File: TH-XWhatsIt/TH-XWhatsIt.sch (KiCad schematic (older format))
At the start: 28 parts, among them J1 MODEL F, J2 EXPANSION, J3 EXPANSION HEADER, SW1 SW_Push, SW2 SW_Push, U1 MCP4921-EP, U2 LM339, U3 74HCT595, U4 74HCT595, U5 ProMicro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

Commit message: Added compact beamspring-only version
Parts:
- removed C7: 0U1, Capacitor_SMD:C_0402_1005Metric, symbol Device:C_Small
- removed H1, H2: GROUND STRAP, MountingHole:MountingHole_4.5mm_Pad_Via, symbol Mechanical:MountingHole_Pad
- removed J2: EXPANSION, TH-XWhatsIt:12-pin-castelated-connector, symbol Connector_Generic:Conn_01x12
- removed RN3: 100K, Resistor_SMD:R_Array_Convex_4x0603, symbol Device:R_Pack04
- removed SW1, SW2: SW_Push, TH-XWhatsIt:PadsToShort, symbol Switch:SW_Push
- removed U6: LM339, Package_SO:SOIC-14_3.9x8.7mm_P1.27mm, symbol Comparator:LM339
- added NT1, NT2: Net-Tie_3, NetTie:NetTie-3_THT_Pad0.3mm, symbol Device:Net-Tie_3
- C1, C2, C3, C4, C5, C6: footprint Capacitor_SMD:C_0402_1005Metric -> Capacitor_SMD:C_0805_2012Metric_Pad1.15x1.40mm_HandSolder
- J1: value MODEL F -> BEAMSPRING CONNECTOR; footprint TH-XWhatsIt:30-pin-castelated-connector -> TH-XWhatsIt:30-pin-universal-beamspring-connector_v2
- R1, R2, R3, R4, R5: footprint Resistor_SMD:R_0402_1005Metric -> Resistor_SMD:R_0805_2012Metric_Pad1.15x1.40mm_HandSolder
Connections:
- net labels removed: COL24, SENSE5, SENSE6, SENSE7, SENSE8
- wire segments 111 -> 78
- no-connect marks 2 -> 4
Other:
- moved on the sheet: J3

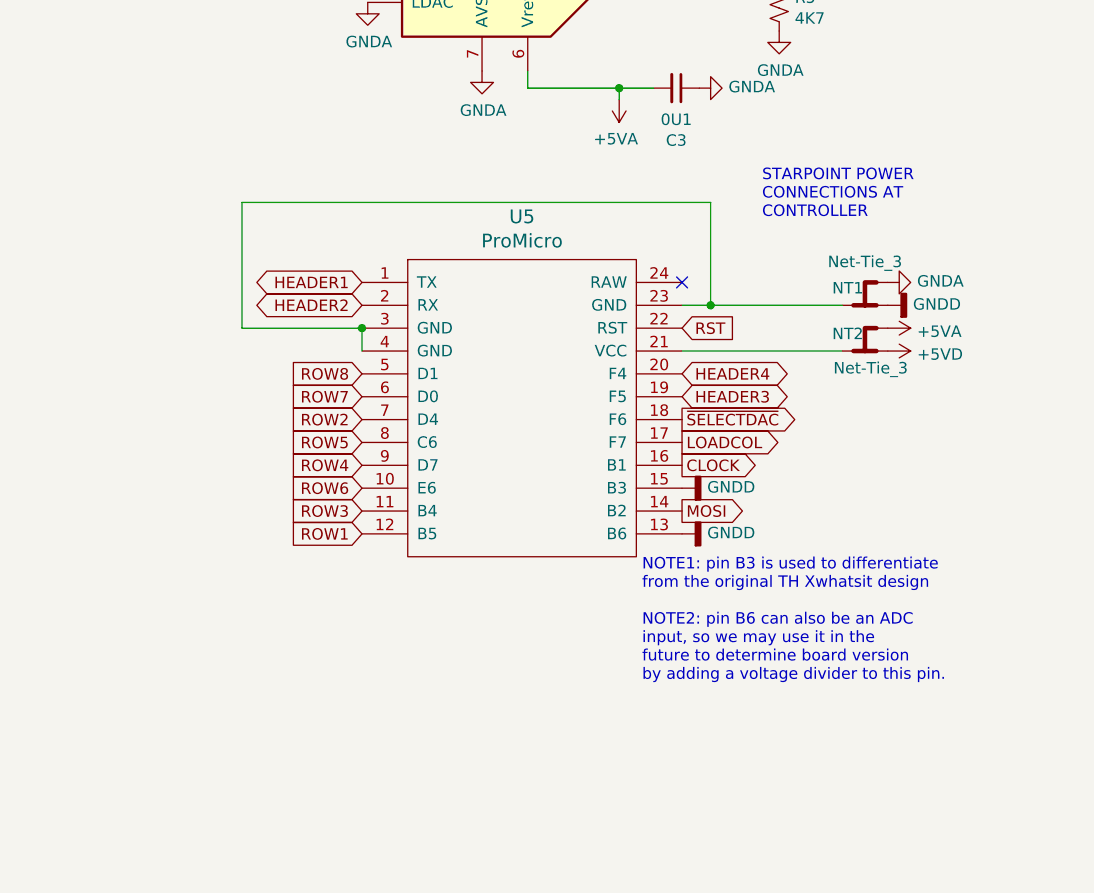
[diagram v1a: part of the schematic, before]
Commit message: added version selection resistor divider pads
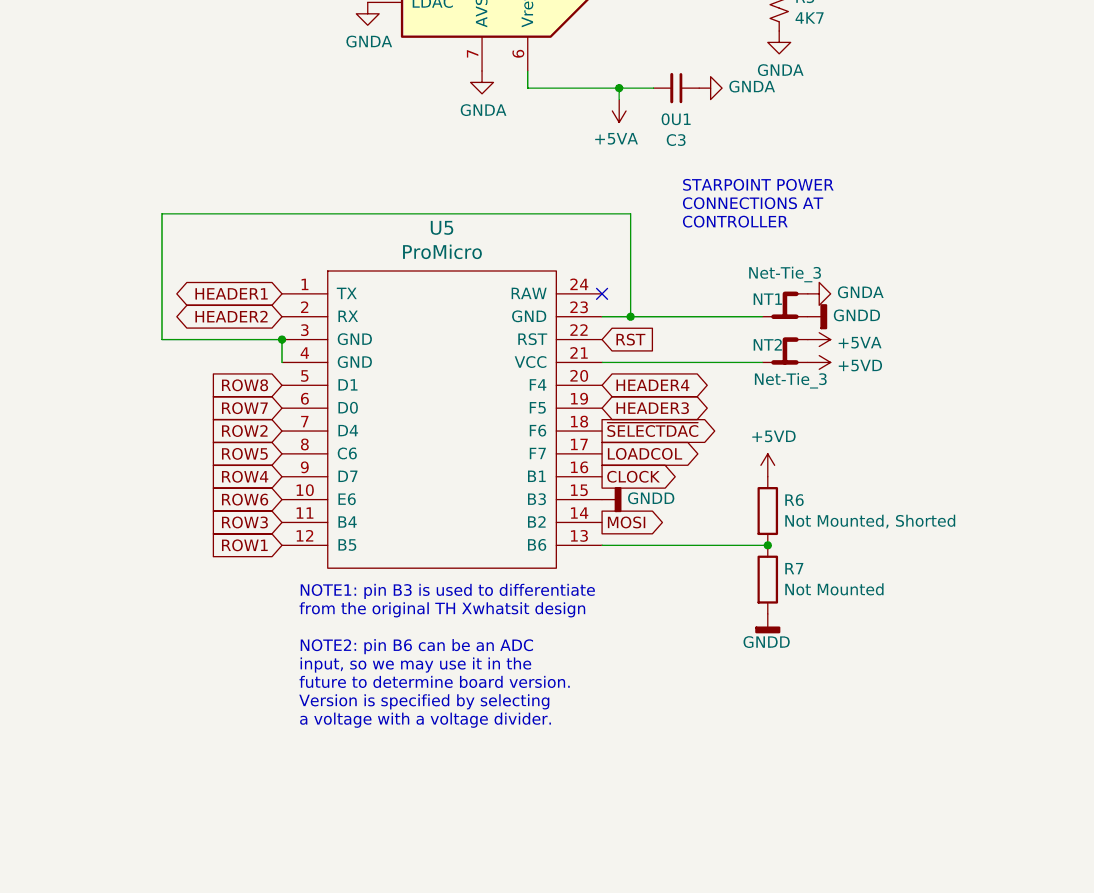
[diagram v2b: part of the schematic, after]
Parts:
- added R6: Not Mounted, Shorted, TH-XWhatsIt:SHORTEDR_0805_2012Metric_Pad1.15x1.40mm_HandSolder, symbol Device:R
- added R7: Not Mounted, Resistor_SMD:R_0805_2012Metric_Pad1.15x1.40mm_HandSolder, symbol Device:R
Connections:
- net +5VD: now also R6.1
- net GNDD: now also R7.2; no longer U5.13 (B6)
- new net: R6.2, R7.1, U5.13 (B6)
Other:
- note added: "NOTE1: pin B3 is used to differentiate\nfrom the original TH Xwhatsit design\n\nNOTE2: pin B6 can be an ADC\ninput, so we may use it in the\nfuture to determine board version.\nVersion is specified by selecting\na voltage with a voltage divider."
- note removed: "NOTE1: pin B3 is used to differentiate\nfrom the original TH Xwhatsit design\n\nNOTE2: pin B6 can also be an ADC\ninput, so we may use it in the\nfuture to determine board version\nby adding a voltage divider to this pin."
- moved on the sheet: NT1, NT2, U5
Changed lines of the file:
@@
 Wire Wire Line
 	10275 1400 10275 1425
-Text GLabel 9850 3525 2    50   Output ~ 0
+Text GLabel 9500 3575 2    50   Output ~ 0
 CLOCK
-NoConn ~ 9850 2725
-Text GLabel 8450 3825 0    50   Input ~ 0
+NoConn ~ 9500 2775
+Text GLabel 8100 3875 0    50   Input ~ 0
 ROW1
-Text GLabel 8450 3325 0    50   Input ~ 0
+Text GLabel 8100 3375 0    50   Input ~ 0
 ROW2
-Text GLabel 8450 3725 0    50   Input ~ 0
+Text GLabel 8100 3775 0    50   Input ~ 0
 ROW3
-Text GLabel 8450 3525 0    50   Input ~ 0
+Text GLabel 8100 3575 0    50   Input ~ 0
 ROW4
-Text GLabel 8450 3425 0    50   Input ~ 0
+Text GLabel 8100 3475 0    50   Input ~ 0
 ROW5
-Text GLabel 8450 3625 0    50   Input ~ 0
+Text GLabel 8100 3675 0    50   Input ~ 0
 ROW6
-Text GLabel 8450 3225 0    50   Input ~ 0
+Text GLabel 8100 3275 0    50   Input ~ 0
 ROW7
-Text GLabel 8450 3125 0    50   Input ~ 0
+Text GLabel 8100 3175 0    50   Input ~ 0
 ROW8
 $Comp
@@
 Text GLabel 3500 2775 2    50   Output ~ 0
 ROW4
-Text GLabel 9850 3425 2    50   Output ~ 0
+Text GLabel 9500 3475 2    50   Output ~ 0
 LOADCOL
 Text GLabel 2675 5875 0    50   Input ~ 0
@@
 Text GLabel 2675 5375 0    50   Input ~ 0
 COL14
-Text GLabel 9850 3725 2    50   Output ~ 0
+Text GLabel 9500 3775 2    50   Output ~ 0
 MOSI
 Text GLabel 8475 1200 0    50   Input ~ 0
@@
 	1    0    0    -1
 $EndComp
-Text GLabel 9850 3325 2    50   Output ~ 0
+Text GLabel 9500 3375 2    50   Output ~ 0
 ~SELECTDAC
 Text GLabel 8475 1400 0    50   Input ~ 0
@@
 L power:+5VD #PWR027
 U 1 1 5E81915B
-P 10750 3025
-F 0 "#PWR027" H 10750 2875 50  0001 C CNN
-F 1 "+5VD" V 10765 3153 50  0000 L CNN
-F 2 "" H 10750 3025 50  0001 C CNN
-F 3 "" H 10750 3025 50  0001 C CNN
-	1    10750 3025
+P 10400 3075
+F 0 "#PWR027" H 10400 2925 50  0001 C CNN
+F 1 "+5VD" V 10415 3203 50  0000 L CNN
+F 2 "" H 10400 3075 50  0001 C CNN
+F 3 "" H 10400 3075 50  0001 C CNN
+	1    10400 3075
 	0    1    1    0
 $EndComp
@@
 L power:GNDD #PWR023
 U 1 1 5E823659
-P 10750 2825
-F 0 "#PWR023" H 10750 2575 50  0001 C CNN
-F 1 "GNDD" V 10754 2715 50  0000 R CNN
-F 2 "" H 10750 2825 50  0001 C CNN
-F 3 "" H 10750 2825 50  0001 C CNN
-	1    10750 2825
+P 10400 2875
+F 0 "#PWR023" H 10400 2625 50  0001 C CNN
+F 1 "GNDD" V 10404 2765 50  0000 R CNN
+F 2 "" H 10400 2875 50  0001 C CNN
+F 3 "" H 10400 2875 50  0001 C CNN
+	1    10400 2875
 	0    -1   -1   0
 $EndComp
@@
 L power:+5VA #PWR025
 U 1 1 5E8BFA71
-P 10750 2925
-F 0 "#PWR025" H 10750 2775 50  0001 C CNN
-F 1 "+5VA" V 10765 3053 50  0000 L CNN
-F 2 "" H 10750 2925 50  0001 C CNN
-F 3 "" H 10750 2925 50  0001 C CNN
-	1    10750 2925
+P 10400 2975
+F 0 "#PWR025" H 10400 2825 50  0001 C CNN
+F 1 "+5VA" V 10415 3103 50  0000 L CNN
+F 2 "" H 10400 2975 50  0001 C CNN
+F 3 "" H 10400 2975 50  0001 C CNN
+	1    10400 2975
 	0    1    1    0
 $EndComp
@@
 L power:GNDA #PWR021
 U 1 1 5E8BFD09
-P 10750 2725
-F 0 "#PWR021" H 10750 2475 50  0001 C CNN
-F 1 "GNDA" V 10755 2597 50  0000 R CNN
-F 2 "" H 10750 2725 50  0001 C CNN
-F 3 "" H 10750 2725 50  0001 C CNN
-	1    10750 2725
-	0    -1   -1   0
-$EndComp
-Wire Wire Line
-	9850 3025 10550 3025
-Wire Wire Line
-	10550 2825 9975 2825
-Text Notes 10200 2450 0    50   ~ 0
+P 10400 2775
+F 0 "#PWR021" H 10400 2525 50  0001 C CNN
+F 1 "GNDA" V 10405 2647 50  0000 R CNN
+F 2 "" H 10400 2775 50  0001 C CNN
+F 3 "" H 10400 2775 50  0001 C CNN
+	1    10400 2775
+	0    -1   -1   0
+$EndComp
+Wire Wire Line
+	9500 3075 10200 3075
+Wire Wire Line
+	10200 2875 9625 2875
+Text Notes 9850 2500 0    50   ~ 0
 STARPOINT POWER\nCONNECTIONS AT\nCONTROLLER
 Text GLabel 2675 3875 0    50   Output ~ 0
@@
 Text GLabel 7125 6100 2    50   BiDi ~ 0
 HEADER4
-Text GLabel 8450 2725 0    50   BiDi ~ 0
+Text GLabel 8100 2775 0    50   BiDi ~ 0
 HEADER1
-Text GLabel 8450 2825 0    50   BiDi ~ 0
+Text GLabel 8100 2875 0    50   BiDi ~ 0
 HEADER2
-Text GLabel 9850 3225 2    50   BiDi ~ 0
+Text GLabel 9500 3275 2    50   BiDi ~ 0
 HEADER3
-Text GLabel 9850 3125 2    50   BiDi ~ 0
+Text GLabel 9500 3175 2    50   BiDi ~ 0
 HEADER4
 Text GLabel 6625 6200 0    50   BiDi ~ 0
@@
 L power:GNDD #PWR0103
 U 1 1 5F4E8027
-P 9850 3625
-F 0 "#PWR0103" H 9850 3375 50  0001 C CNN
-F 1 "GNDD" V 9854 3515 50  0000 R CNN
-F 2 "" H 9850 3625 50  0001 C CNN
-F 3 "" H 9850 3625 50  0001 C CNN
-	1    9850 3625
+P 9500 3675
+F 0 "#PWR0103" H 9500 3425 50  0001 C CNN
+F 1 "GNDD" V 9504 3565 50  0000 R CNN
+F 2 "" H 9500 3675 50  0001 C CNN
+F 3 "" H 9500 3675 50  0001 C CNN
+	1    9500 3675
 	0    -1   -1   0
 $EndComp
@@
 L promicro:ProMicro U5
 U 1 1 5E3248FF
-P 9150 3475
-F 0 "U5" H 9150 4512 60  0000 C CNN
-F 1 "ProMicro" H 9150 4406 60  0000 C CNN
-F 2 "promicro:ProMicro" H 9250 2425 60  0001 C CNN
-F 3 "" H 9250 2425 60  0000 C CNN
-	1    9150 3475
+P 8800 3525
+F 0 "U5" H 8800 4562 60  0000 C CNN
+F 1 "ProMicro" H 8800 4456 60  0000 C CNN
+F 2 "promicro:ProMicro" H 8900 2475 60  0001 C CNN
+F 3 "" H 8900 2475 60  0000 C CNN
+	1    8800 3525
 	1    0    0    -1
 $EndComp
@@
 L power:GNDD #PWR0107
 U 1 1 5F3A2D72
-P 9850 3825
-F 0 "#PWR0107" H 9850 3575 50  0001 C CNN
-F 1 "GNDD" V 9854 3715 50  0000 R CNN
-F 2 "" H 9850 3825 50  0001 C CNN
-F 3 "" H 9850 3825 50  0001 C CNN
-	1    9850 3825
-	0    -1   -1   0
-$EndComp
-Text Notes 9675 4475 0    50   ~ 0
-NOTE1: pin B3 is used to differentiate\nfrom the original TH Xwhatsit design\n\nNOTE2: pin B6 can also be an ADC\ninput, so we may use it in the\nfuture to determine board version\nby adding a voltage divider to this pin.
-Text GLabel 9850 2925 2    50   Input ~ 0
+P 10225 4175
+F 0 "#PWR0107" H 10225 3925 50  0001 C CNN
+F 1 "GNDD" H 10325 4050 50  0000 R CNN
+F 2 "" H 10225 4175 50  0001 C CNN
+F 3 "" H 10225 4175 50  0001 C CNN
+	1    10225 4175
+	1    0    0    -1
+$EndComp
+Text Notes 8175 4675 0    50   ~ 0
+NOTE1: pin B3 is used to differentiate\nfrom the original TH Xwhatsit design\n\nNOTE2: pin B6 can be an ADC\ninput, so we may use it in the\nfuture to determine board version.\nVersion is specified by selecting\na voltage with a voltage divider.
+Text GLabel 9500 2975 2    50   Input ~ 0
 RST
 $Comp
@@
 L Device:Net-Tie_3 NT1
 U 1 1 5F6D07D8
-P 10650 2825
-F 0 "NT1" H 10725 2750 50  0000 C CNN
-F 1 "Net-Tie_3" H 10650 2635 50  0000 C CNN
-F 2 "NetTie:NetTie-3_THT_Pad0.3mm" H 10650 2825 50  0001 C CNN
-F 3 "~" H 10650 2825 50  0001 C CNN
-	1    10650 2825
+P 10300 2875
+F 0 "NT1" H 10375 2800 50  0000 C CNN
+F 1 "Net-Tie_3" H 10300 2685 50  0000 C CNN
+F 2 "NetTie:NetTie-3_THT_Pad0.3mm" H 10300 2875 50  0001 C CNN
+F 3 "~" H 10300 2875 50  0001 C CNN
+	1    10300 2875
 	-1   0    0    1
 $EndComp
@@
 L Device:Net-Tie_3 NT2
 U 1 1 5F6D1B28
-P 10650 3025
-F 0 "NT2" H 10725 2950 50  0000 C CNN
-F 1 "Net-Tie_3" H 10625 3100 50  0000 C CNN
-F 2 "NetTie:NetTie-3_THT_Pad0.3mm" H 10650 3025 50  0001 C CNN
-F 3 "~" H 10650 3025 50  0001 C CNN
-	1    10650 3025
+P 10300 3075
+F 0 "NT2" H 10375 3000 50  0000 C CNN
+F 1 "Net-Tie_3" H 10275 3150 50  0000 C CNN
+F 2 "NetTie:NetTie-3_THT_Pad0.3mm" H 10300 3075 50  0001 C CNN
+F 3 "~" H 10300 3075 50  0001 C CNN
+	1    10300 3075
 	-1   0    0    1
 $EndComp
 Wire Wire Line
-	8450 3025 8450 2925
-Wire Wire Line
-	8450 2925 7925 2925
-Wire Wire Line
-	7925 2925 7925 2375
-Wire Wire Line
-	7925 2375 9975 2375
-Wire Wire Line
-	9975 2375 9975 2825
-Connection ~ 8450 2925
-Connection ~ 9975 2825
-Wire Wire Line
-	9975 2825 9850 2825
+	8100 3075 8100 2975
+Wire Wire Line
+	8100 2975 7575 2975
+Wire Wire Line
+	7575 2975 7575 2425
+Wire Wire Line
+	7575 2425 9625 2425
+Wire Wire Line
+	9625 2425 9625 2875
+Connection ~ 8100 2975
+Connection ~ 9625 2875
+Wire Wire Line
+	9625 2875 9500 2875
+$Comp
+L Device:R R6
+U 1 1 5F3A43C9
+P 10225 3725
+F 0 "R6" H 10295 3771 50  0000 L CNN
+F 1 "Not Mounted, Shorted" H 10295 3680 50  0000 L CNN
+F 2 "TH-XWhatsIt:SHORTEDR_0805_2012Metric_Pad1.15x1.40mm_HandSolder" V 10155 3725 50  0001 C CNN
+F 3 "~" H 10225 3725 50  0001 C CNN
+	1    10225 3725
+	1    0    0    -1
+$EndComp
+$Comp
+L Device:R R7
+U 1 1 5F3A4C74
+P 10225 4025
+F 0 "R7" H 10295 4071 50  0000 L CNN
+F 1 "Not Mounted" H 10295 3980 50  0000 L CNN
+F 2 "Resistor_SMD:R_0805_2012Metric_Pad1.15x1.40mm_HandSolder" V 10155 4025 50  0001 C CNN
+F 3 "~" H 10225 4025 50  0001 C CNN
+	1    10225 4025
+	1    0    0    -1
+$EndComp
+Wire Wire Line
+	10225 3875 9500 3875
+Connection ~ 10225 3875
+$Comp
+L power:+5VD #PWR04
+U 1 1 5F3A9745
+P 10225 3575
+F 0 "#PWR04" H 10225 3425 50  0001 C CNN
+F 1 "+5VD" H 10150 3750 50  0000 L CNN
+F 2 "" H 10225 3575 50  0001 C CNN
+F 3 "" H 10225 3575 50  0001 C CNN
+	1    10225 3575
+	1    0    0    -1
+$EndComp
 $EndSCHEMATC

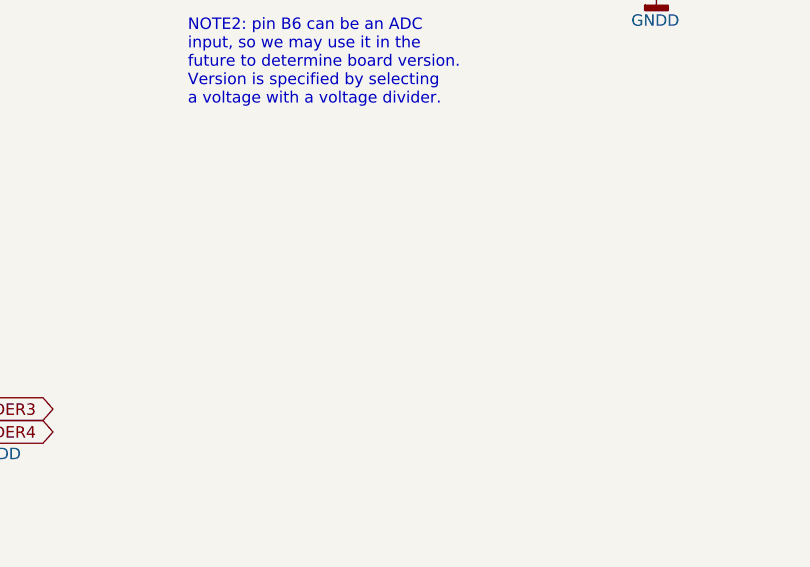
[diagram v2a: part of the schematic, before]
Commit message: Added chassis ground, and added some silkscreen
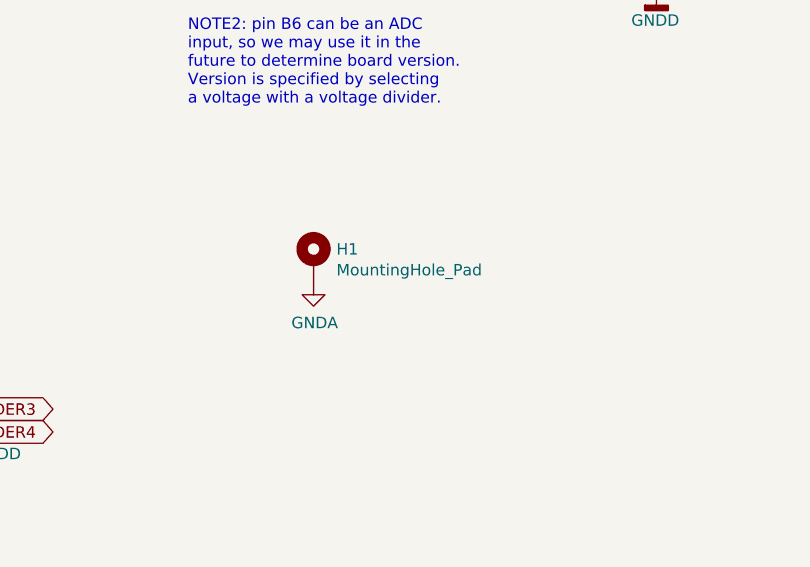
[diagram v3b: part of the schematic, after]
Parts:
- added H1: MountingHole_Pad, TH-XWhatsIt:ChassisGnd, symbol Mechanical:MountingHole_Pad
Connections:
- net GNDA: now also H1.1
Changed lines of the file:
@@
+	1    0    0    -1
+$EndComp
+$Comp
+L Mechanical:MountingHole_Pad H1
+U 1 1 5F40984F
+P 8725 5350
+F 0 "H1" H 8825 5399 50  0000 L CNN
+F 1 "MountingHole_Pad" H 8825 5308 50  0000 L CNN
+F 2 "TH-XWhatsIt:ChassisGnd" H 8725 5350 50  0001 C CNN
+F 3 "~" H 8725 5350 50  0001 C CNN
+	1    8725 5350
+	1    0    0    -1
+$EndComp
+$Comp
+L power:GNDA #PWR06
+U 1 1 5F40CF6A
+P 8725 5450
+F 0 "#PWR06" H 8725 5200 50  0001 C CNN
+F 1 "GNDA" H 8730 5277 50  0000 C CNN
+F 2 "" H 8725 5450 50  0001 C CNN
+F 3 "" H 8725 5450 50  0001 C CNN
+	1    8725 5450
 	1    0    0    -1
 $EndComp

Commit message: added lcsc part number to a bunch of components. Still todo: comparator and 74hc595
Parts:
- C1, C2, C3, C4, C5, C6: LCSC (none) -> C49678
- R1, R5: LCSC (none) -> C17673
- R2: LCSC (none) -> C17513
- R3, R4: LCSC (none) -> C4328
- RN1: LCSC (none) -> C173315
- U1: LCSC (none) -> C43499
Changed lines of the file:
@@
 F 2 "Capacitor_SMD:C_0805_2012Metric_Pad1.15x1.40mm_HandSolder" H 4625 975 50  0001 C CNN
 F 3 "~" H 4625 975 50  0001 C CNN
+F 4 "C49678" H 4625 975 50  0001 C CNN "LCSC"
 	1    4625 975
 	0    -1   -1   0
@@
 F 2 "Capacitor_SMD:C_0805_2012Metric_Pad1.15x1.40mm_HandSolder" H 1350 6950 50  0001 C CNN
 F 3 "~" H 1350 6950 50  0001 C CNN
+F 4 "C49678" H 1350 6950 50  0001 C CNN "LCSC"
 	1    1350 6950
 	0    -1   -1   0
@@
 F 2 "Resistor_SMD:R_0805_2012Metric_Pad1.15x1.40mm_HandSolder" H 10150 1400 50  0001 C CNN
 F 3 "~" H 10150 1400 50  0001 C CNN
+F 4 "C4328" H 10150 1400 50  0001 C CNN "LCSC"
 	1    10150 1400
 	0    1    1    0
@@
 F 2 "Resistor_SMD:R_0805_2012Metric_Pad1.15x1.40mm_HandSolder" H 10275 1275 50  0001 C CNN
 F 3 "~" H 10275 1275 50  0001 C CNN
+F 4 "C4328" H 10275 1275 50  0001 C CNN "LCSC"
 	1    10275 1275
 	-1   0    0    1
@@
 F 2 "Resistor_SMD:R_0805_2012Metric_Pad1.15x1.40mm_HandSolder" H 10275 1525 50  0001 C CNN
 F 3 "~" H 10275 1525 50  0001 C CNN
+F 4 "C17673" H 10275 1525 50  0001 C CNN "LCSC"
 	1    10275 1525
 	-1   0    0    1
@@
 F 2 "Capacitor_SMD:C_0805_2012Metric_Pad1.15x1.40mm_HandSolder" H 4625 4525 50  0001 C CNN
 F 3 "~" H 4625 4525 50  0001 C CNN
+F 4 "C49678" H 4625 4525 50  0001 C CNN "LCSC"
 	1    4625 4525
 	0    -1   -1   0
@@
 F 2 "Resistor_SMD:R_0805_2012Metric_Pad1.15x1.40mm_HandSolder" H 4350 6125 50  0001 C CNN
 F 3 "~" H 4350 6125 50  0001 C CNN
+F 4 "C17673" H 4350 6125 50  0001 C CNN "LCSC"
 	1    4350 6125
 	1    0    0    -1
@@
 F 2 "Resistor_SMD:R_0805_2012Metric_Pad1.15x1.40mm_HandSolder" H 4350 6375 50  0001 C CNN
 F 3 "~" H 4350 6375 50  0001 C CNN
+F 4 "C17513" H 4350 6375 50  0001 C CNN "LCSC"
 	1    4350 6375
 	-1   0    0    1
@@
 F 2 "Package_SO:SOIC-8_3.9x4.9mm_P1.27mm" H 9075 1400 50  0001 C CIN
 F 3 "http://ww1.microchip.com/downloads/en/devicedoc/21897a.pdf" H 9075 1400 50  0001 C CNN
+F 4 "C43499" H 9075 1400 50  0001 C CNN "LCSC"
 	1    9075 1400
 	1    0    0    -1
@@
 F 2 "Capacitor_SMD:C_0805_2012Metric_Pad1.15x1.40mm_HandSolder" H 9825 1875 50  0001 C CNN
 F 3 "~" H 9825 1875 50  0001 C CNN
+F 4 "C49678" H 9825 1875 50  0001 C CNN "LCSC"
 	1    9825 1875
 	0    1    1    0
@@
 F 2 "Capacitor_SMD:C_0805_2012Metric_Pad1.15x1.40mm_HandSolder" H 8325 925 50  0001 C CNN
 F 3 "~" H 8325 925 50  0001 C CNN
+F 4 "C49678" H 8325 925 50  0001 C CNN "LCSC"
 	1    8325 925
 	0    -1   -1   0
@@
 F 2 "Resistor_SMD:R_Array_Convex_4x0603" V 1800 1175 50  0001 C CNN
 F 3 "~" H 1525 1175 50  0001 C CNN
+F 4 "C173315" H 1525 1175 50  0001 C CNN "LCSC"
 	1    1525 1175
 	1    0    0    1
@@
 F 2 "Capacitor_SMD:C_0805_2012Metric_Pad1.15x1.40mm_HandSolder" H 4625 2750 50  0001 C CNN
 F 3 "~" H 4625 2750 50  0001 C CNN
+F 4 "C49678" H 4625 2750 50  0001 C CNN "LCSC"
 	1    4625 2750
 	0    -1   -1   0
